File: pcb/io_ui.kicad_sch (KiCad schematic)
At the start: 45 parts, among them J10 UART, J4 Digital IO, J5 ADC Inputs, J8 I2C Bus, Q4 2N7002, Q5 2N7002, U8 24AA64T

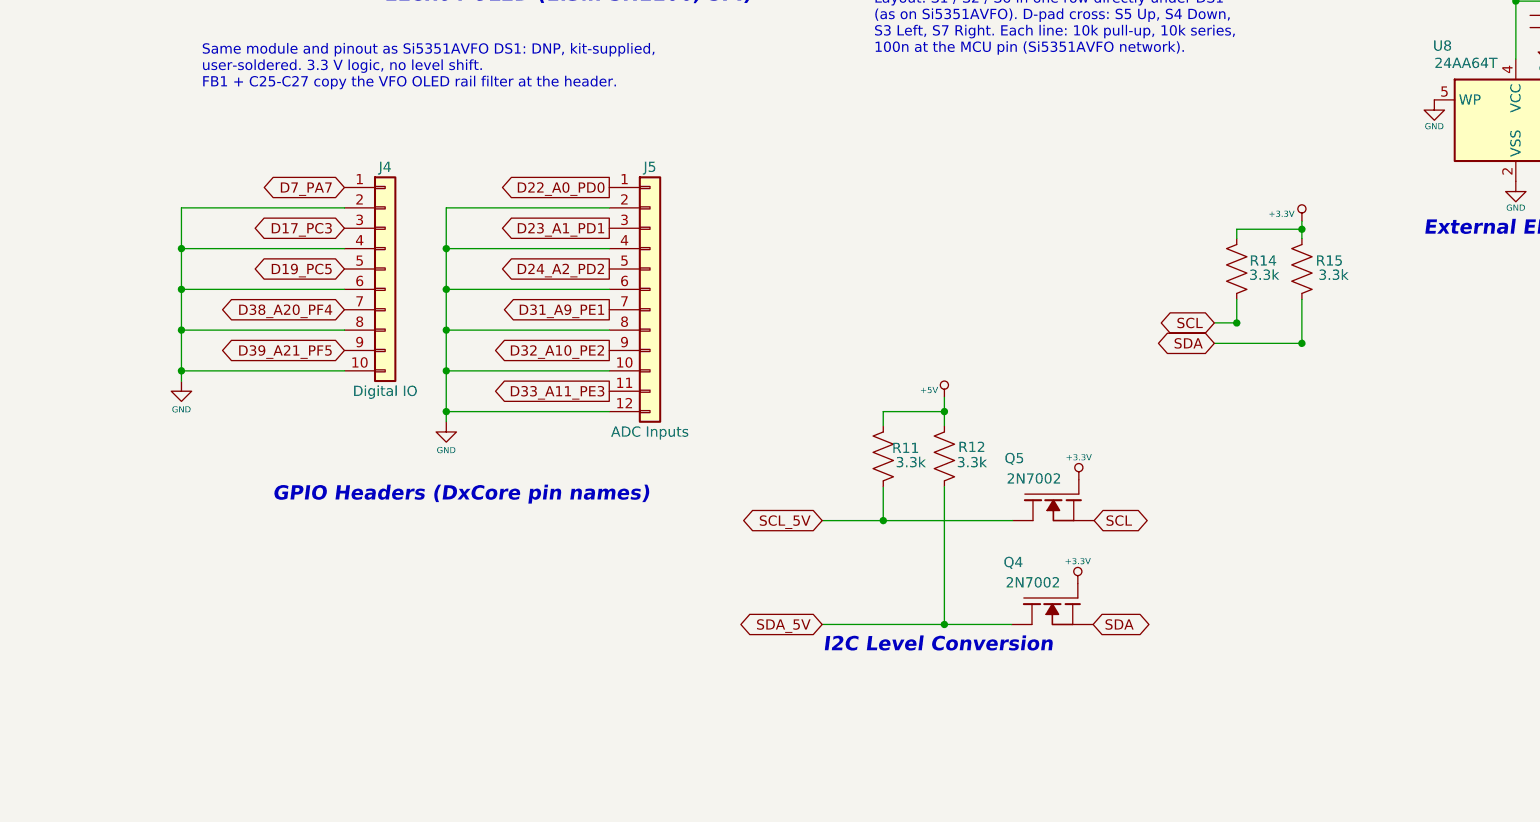
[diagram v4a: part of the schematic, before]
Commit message: ESD: SP0503BAHT (C7074, already on BOM) at J4/J5 header pins + J14 PPS with 220R series (R64-R75, 0805 C17557 basic); ESD5V3U1U-02LRH (C3011174) on GPS RF_IN at U.FL J15; J5 moved under J4, header-side nets HDR_Dn; I2C level shift block moved right; regen PDF
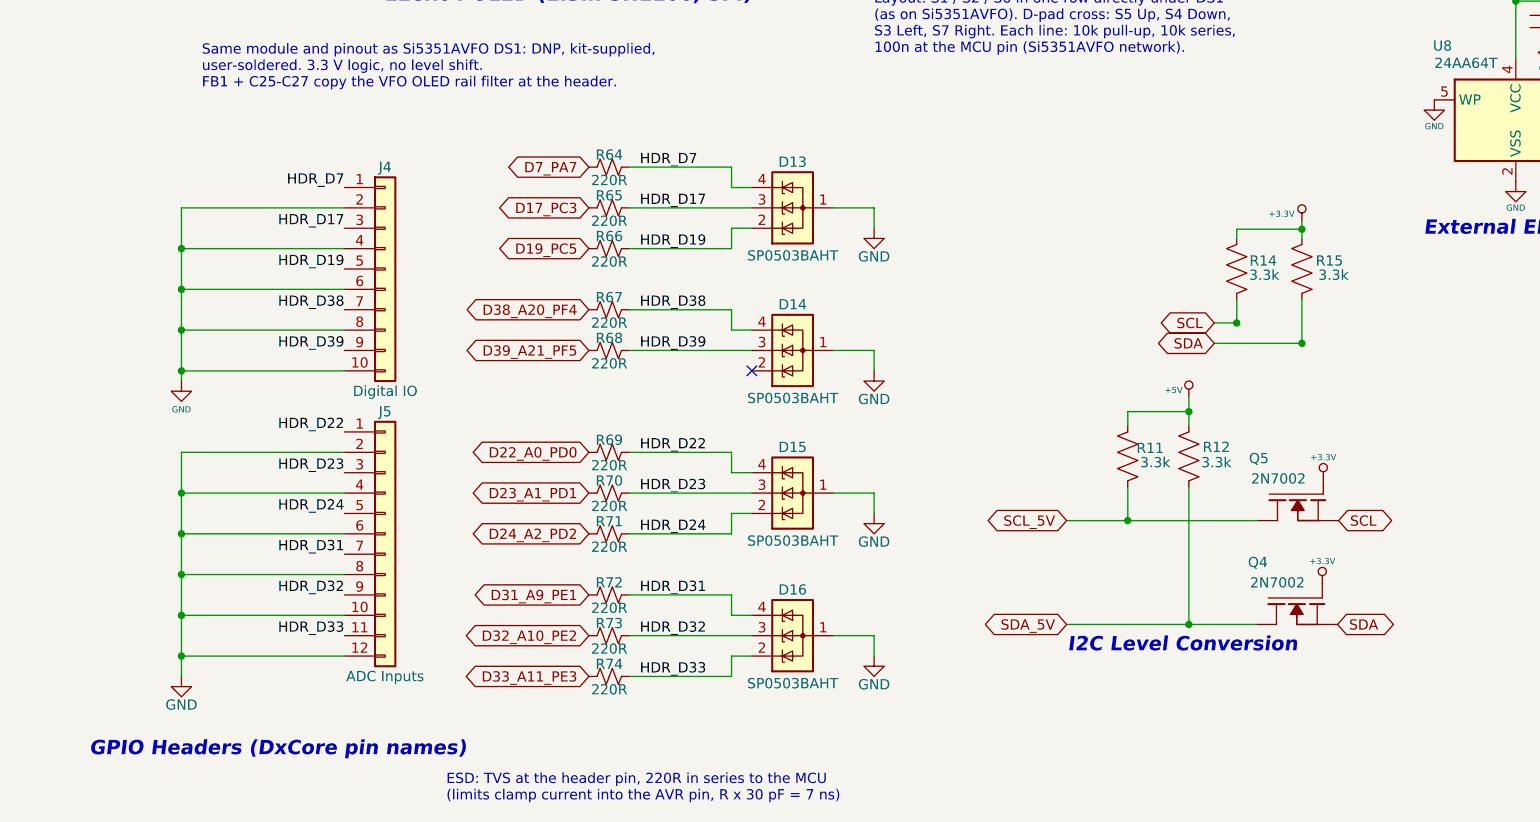
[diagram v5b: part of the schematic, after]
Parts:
- added D13, D14, D15, D16: SP0503BAHT, Package_TO_SOT_SMD:SOT-143, symbol Power_Protection:SP0503BAHT
- added R64, R65, R66, R67, R68, R69, R70, R71, R72, R73, R74: 220R, Resistor_SMD:R_0805_2012Metric, symbol Device:R_Small_US
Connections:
- net D17_PC3: now also R65.1; no longer J4.3 (Pin_3)
- net D19_PC5: now also R66.1; no longer J4.5 (Pin_5)
- net D22_A0_PD0: now also R69.1; no longer J5.1 (Pin_1)
- net D23_A1_PD1: now also R70.1; no longer J5.3 (Pin_3)
- net D24_A2_PD2: now also R71.1; no longer J5.5 (Pin_5)
- net D31_A9_PE1: now also R72.1; no longer J5.7 (Pin_7)
- net D32_A10_PE2: now also R73.1; no longer J5.9 (Pin_9)
- net D33_A11_PE3: now also R74.1; no longer J5.11 (Pin_11)
- net D38_A20_PF4: now also R67.1; no longer J4.7 (Pin_7)
- net D39_A21_PF5: now also R68.1; no longer J4.9 (Pin_9)
- net D7_PA7: now also R64.1; no longer J4.1 (Pin_1)
- net GND: now also D13.1 (A), D14.1 (A), D15.1 (A), D16.1 (A)
- new net HDR_D17: D13.3 (K), J4.3 (Pin_3), R65.2
- new net HDR_D19: D13.2 (K), J4.5 (Pin_5), R66.2
- new net HDR_D22: D15.4 (K), J5.1 (Pin_1), R69.2
- new net HDR_D23: D15.3 (K), J5.3 (Pin_3), R70.2
- new net HDR_D24: D15.2 (K), J5.5 (Pin_5), R71.2
- new net HDR_D31: D16.4 (K), J5.7 (Pin_7), R72.2
- new net HDR_D32: D16.3 (K), J5.9 (Pin_9), R73.2
- new net HDR_D33: D16.2 (K), J5.11 (Pin_11), R74.2
- new net HDR_D38: D14.4 (K), J4.7 (Pin_7), R67.2
- new net HDR_D39: D14.3 (K), J4.9 (Pin_9), R68.2
- new net HDR_D7: D13.4 (K), J4.1 (Pin_1), R64.2
- no-connect marks 0 -> 1
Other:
- note added: "ESD: TVS at the header pin, 220R in series to the MCU (limits clamp current into the AVR pin, R x 30 pF = 7 ns)"
- moved on the sheet: J5, Q4, Q5, R11, R12

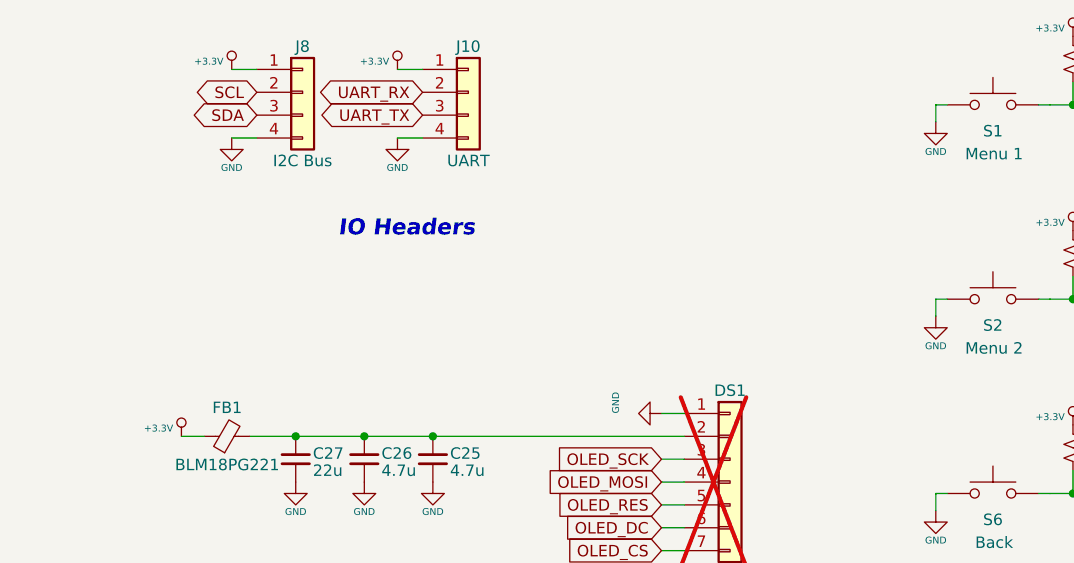
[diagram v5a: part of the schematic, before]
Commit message: ESD: SP0503BAHT (C7074) on J8 I2C (D19) and J10 UART (D20) with 220R series R76-R79 (C17557), header-side nets HDR_SCL/SDA/RX/TX; ESD5V3U1U-02LRH (C3011174) D21 on J16 CLKIN SMA, net CLKIN_SMA; regen PDF
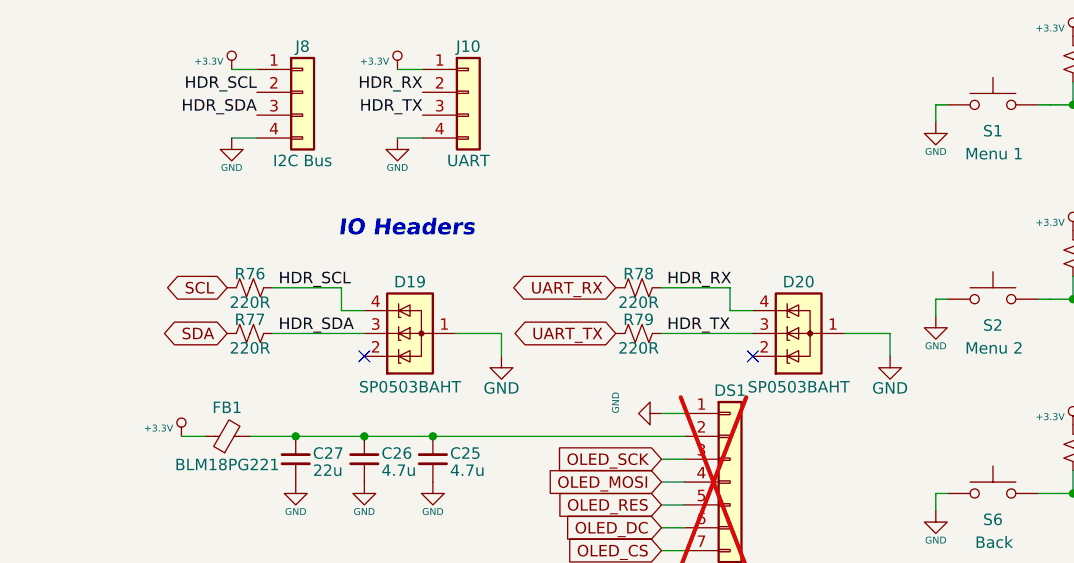
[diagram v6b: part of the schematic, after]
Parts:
- added D19, D20: SP0503BAHT, Package_TO_SOT_SMD:SOT-143, symbol Power_Protection:SP0503BAHT
- added R76, R77, R78, R79: 220R, Resistor_SMD:R_0805_2012Metric, symbol Device:R_Small_US
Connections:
- net GND: now also D19.1 (A), D20.1 (A)
- net SCL: now also R76.1; no longer J8.2 (Pin_2)
- net SDA: now also R77.1; no longer J8.3 (Pin_3)
- net UART_RX: now also R78.1; no longer J10.2 (Pin_2)
- net UART_TX: now also R79.1; no longer J10.3 (Pin_3)
- new net HDR_RX: D20.4 (K), J10.2 (Pin_2), R78.2
- new net HDR_SCL: D19.4 (K), J8.2 (Pin_2), R76.2
- new net HDR_SDA: D19.3 (K), J8.3 (Pin_3), R77.2
- new net HDR_TX: D20.3 (K), J10.3 (Pin_3), R79.2
- no-connect marks 1 -> 3

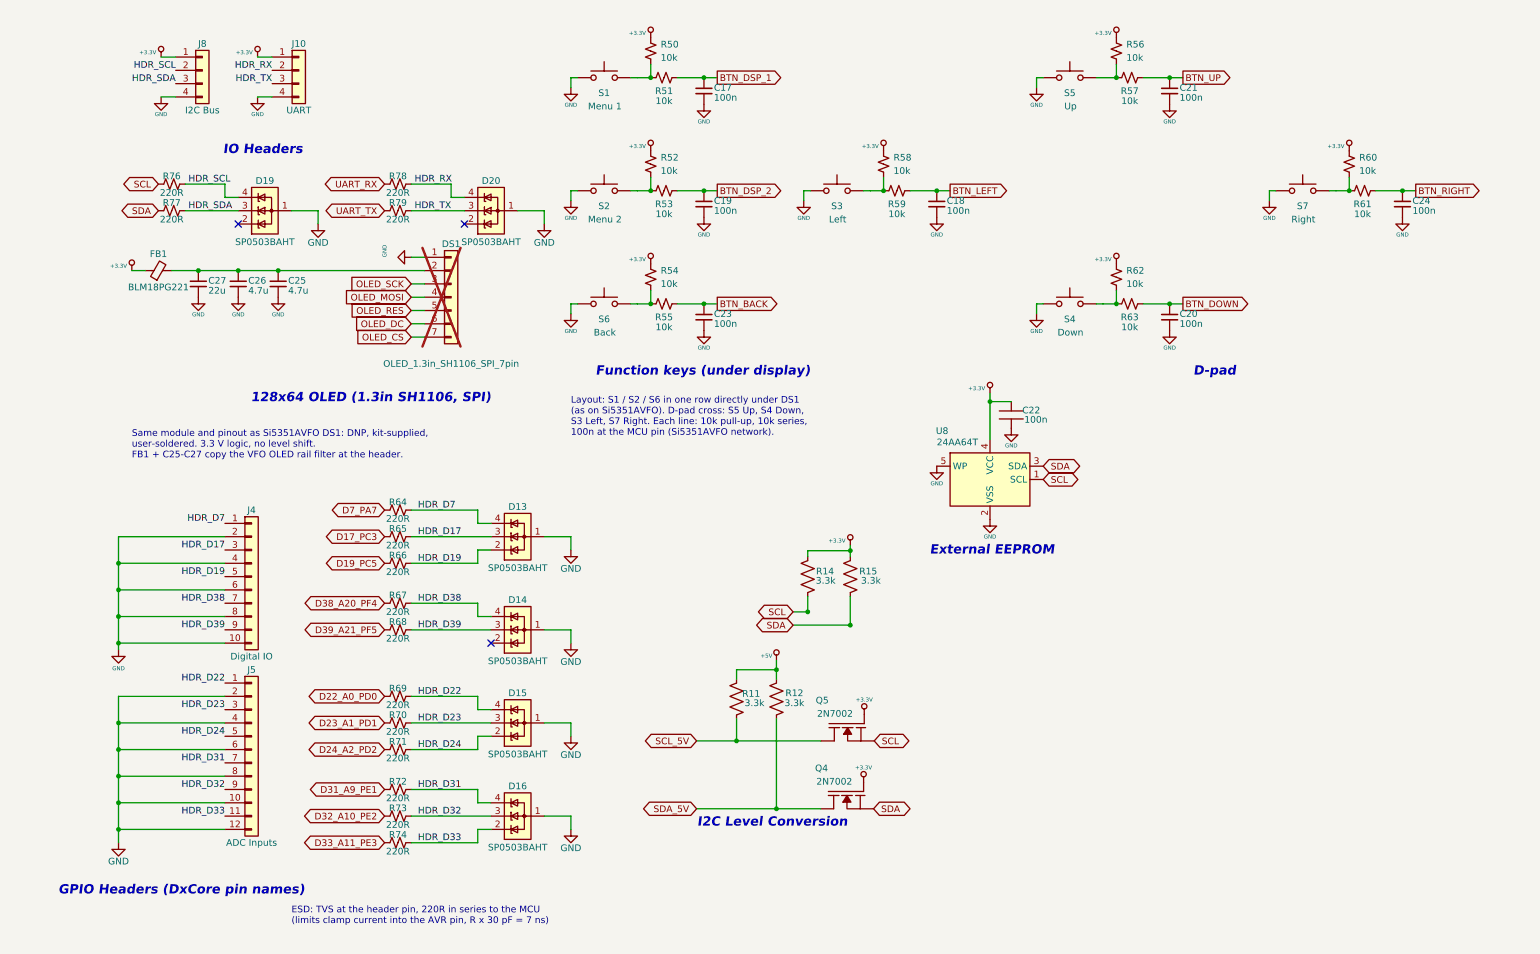
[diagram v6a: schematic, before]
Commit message: Schematic style: pages 1-2 (root, I/O+UI) functional blocks in dashed boxes with titles and notes, matching other sheets; Si5351C block up 12.7 mm, PA/bias/filter-bank band down 6.35 mm, boost down 2.54 mm, EEPROM moved right, OLED down 5.08 mm; no connectivity change (netlist identical); regen PDF
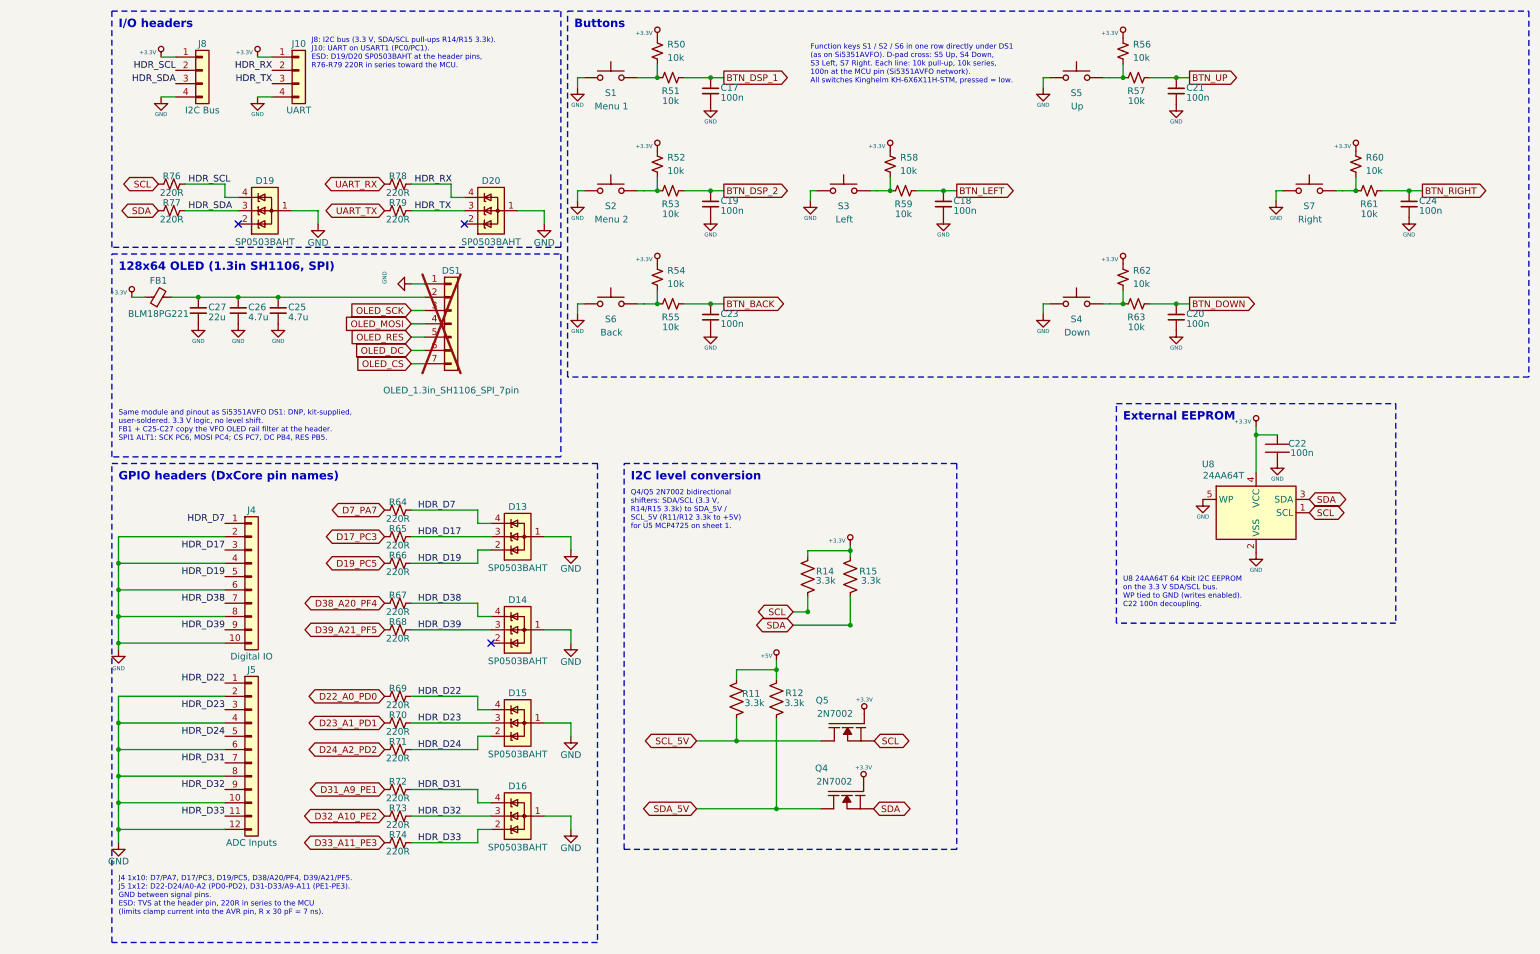
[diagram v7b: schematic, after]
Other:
- note added: "Buttons"
- note added: "Function keys S1 / S2 / S6 in one row directly under DS1 (as on Si5351AVFO). D-pad cross: S5 Up, S4 Down, S3 Left, S7 Right. Each line: 10k pull-up, 10k series, 100n at the MCU pin (Si5351AVFO network). All switches Kinghelm KH-6X6X11H-STM, pressed = low."
- note added: "GPIO headers (DxCore pin names)"
- note added: "I/O headers"
- note added: "I2C level conversion"
- note added: "J4 1x10: D7/PA7, D17/PC3, D19/PC5, D38/A20/PF4, D39/A21/PF5. J5 1x12: D22-D24/A0-A2 (PD0-PD2), D31-D33/A9-A11 (PE1-PE3). GND between signal pins. ESD: TVS at the header pin, 220R in series to the MCU (limits clamp current into the AVR pin, R x 30 pF = 7 ns)."
- note added: "J8: I2C bus (3.3 V, SDA/SCL pull-ups R14/R15 3.3k). J10: UART on USART1 (PC0/PC1). ESD: D19/D20 SP0503BAHT at the header pins, R76-R79 220R in series toward the MCU."
- note added: "Q4/Q5 2N7002 bidirectional shifters: SDA/SCL (3.3 V, R14/R15 3.3k) to SDA_5V / SCL_5V (R11/R12 3.3k to +5V) for U5 MCP4725 on sheet 1."
- note added: "Same module and pinout as Si5351AVFO DS1: DNP, kit-supplied, user-soldered. 3.3 V logic, no level shift. FB1 + C25-C27 copy the VFO OLED rail filter at the header. SPI1 ALT1: SCK PC6, MOSI PC4; CS PC7, DC PB4, RES PB5."
- note added: "U8 24AA64T 64 Kbit I2C EEPROM on the 3.3 V SDA/SCL bus. WP tied to GND (writes enabled). C22 100n decoupling."
- note removed: "D-pad"
- note removed: "ESD: TVS at the header pin, 220R in series to the MCU (limits clamp current into the AVR pin, R x 30 pF = 7 ns)"
- note removed: "Function keys (under display)"
- note removed: "GPIO Headers (DxCore pin names)"
- note removed: "I2C Level Conversion"
- note removed: "IO Headers"
- note removed: "Layout: S1 / S2 / S6 in one row directly under DS1 (as on Si5351AVFO). D-pad cross: S5 Up, S4 Down, S3 Left, S7 Right. Each line: 10k pull-up, 10k series, 100n at the MCU pin (Si5351AVFO network)."
- note removed: "Same module and pinout as Si5351AVFO DS1: DNP, kit-supplied, user-soldered. 3.3 V logic, no level shift. FB1 + C25-C27 copy the VFO OLED rail filter at the header."
- moved on the sheet: C17, C18, C19, C20, C21, C22, C23, C24, C25, C26, C27, DS1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
